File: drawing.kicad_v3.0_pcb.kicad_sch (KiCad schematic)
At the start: 43 parts, among them IC1 DW01A-G, J1 Micro USB Chargeport, J2 Conn_01x03, J3 128x32 I2C OLED, J4 TP4056, J5 MK-12C02, J6 Conn_01x02, Q1 FS8205, U1 HT7333-SOT89, U2 ESP-12E, U3 ATTINY85-20PU

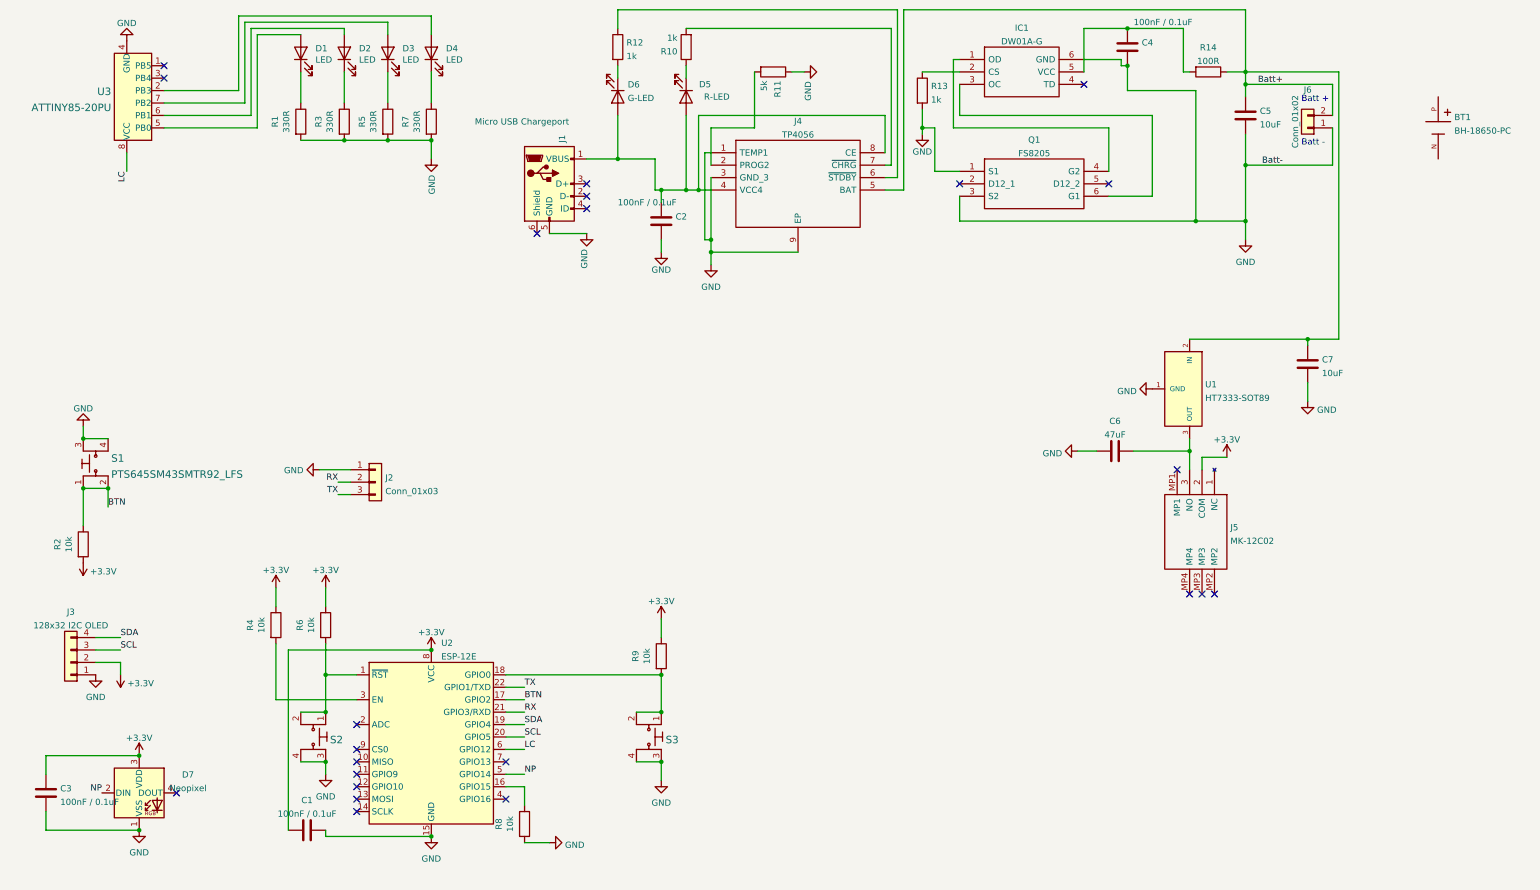
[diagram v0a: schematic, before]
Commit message: Fixed HT7333 and charging circuit
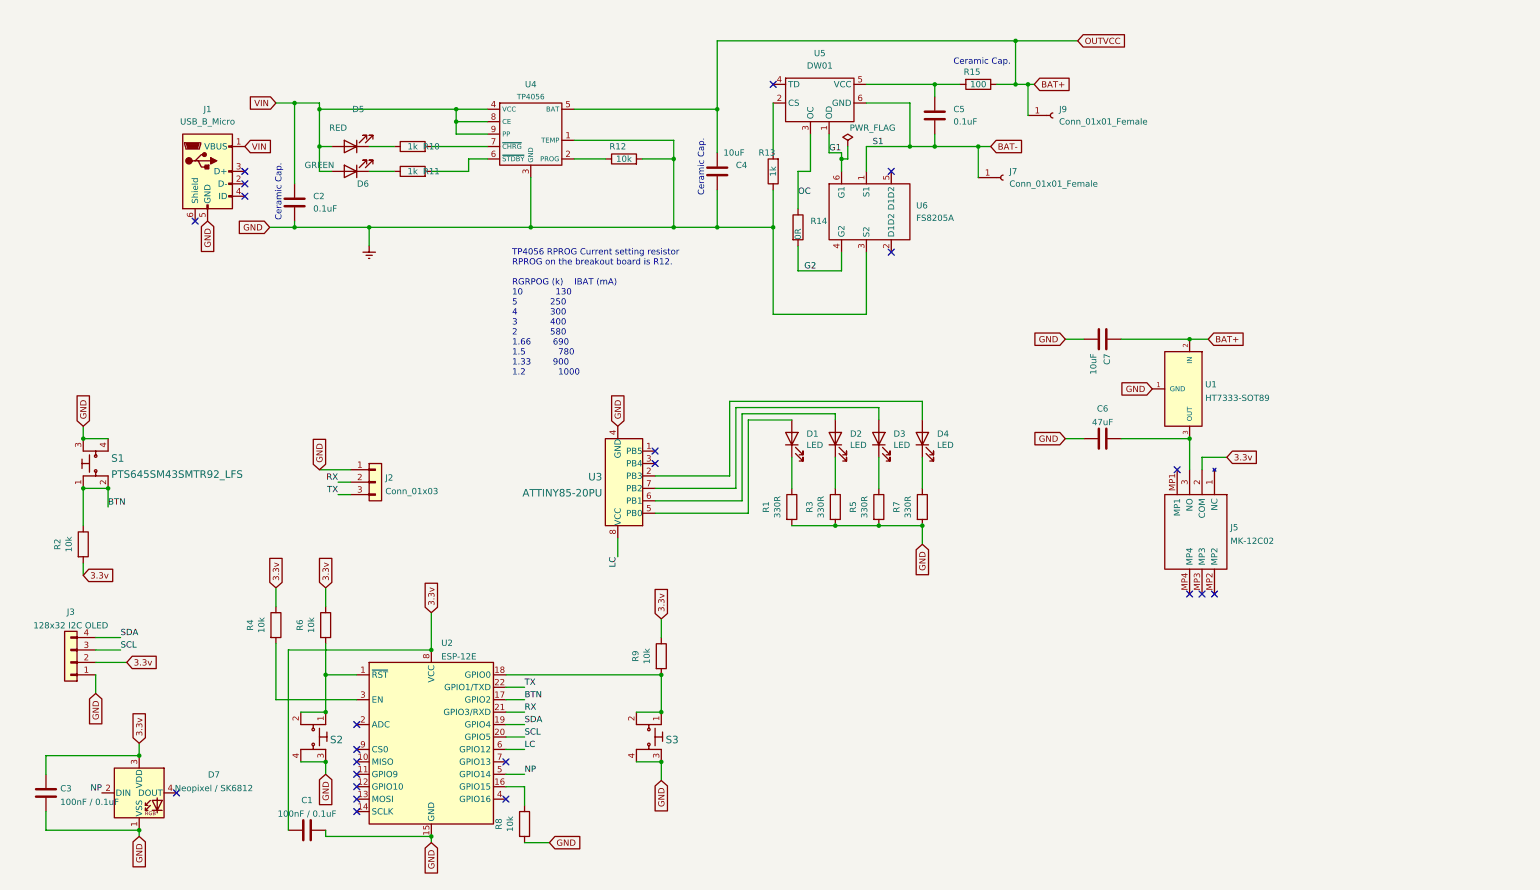
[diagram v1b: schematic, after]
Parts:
- removed BT1: BH-18650-PC, user-footprints:BAT_BH-18650-PC, symbol BH-18650-PC:BH-18650-PC
- removed IC1: DW01A-G, user-footprints:SOT95P280X135-6N, symbol DW01A-G:DW01A-G
- removed J4: TP4056, Custom:SOIC127P600X175-9N, symbol TP4056:TP4056
- removed J6: Conn_01x02, Connector_PinSocket_2.54mm:PinSocket_1x02_P2.54mm_Vertical, symbol Connector_Generic:Conn_01x02
- removed Q1: FS8205, user-footprints:FS8205, symbol FS8205:FS8205
- added J7, J9: Conn_01x01_Female, Connector_PinSocket_2.54mm:PinSocket_1x01_P2.54mm_Vertical, symbol Connector:Conn_01x01_Female
- added R15: 100, Resistor_SMD:R_0805_2012Metric_Pad1.20x1.40mm_HandSolder, symbol Device:R
- added U4: TP4056, Package_SO:SOIC-8-1EP_3.9x4.9mm_P1.27mm_EP2.29x3mm, symbol tp4056:TP4056
- added U5: DW01, Package_TO_SOT_SMD:SOT-23-6_Handsoldering, symbol dw01:DW01
- added U6: FS8205A, Package_TO_SOT_SMD:SOT-23-6_Handsoldering, symbol fs8205:FS8205A
- C2: value 100nF / 0.1uF -> 0.1uF
- C4: value 100nF / 0.1uF -> 10uF
- C5: value 10uF -> 0.1uF
- D5: value R-LED -> RED
- D6: value G-LED -> GREEN
- D7: value Neopixel -> Neopixel / SK6812
- J1: value Micro USB Chargeport -> USB_B_Micro
- R11: value 5k -> 1k
- R12: value 1k -> 10k
- R14: value 100R -> 0R
- U1: footprint Custom:Holtek-HT7333-SOT89-Level_A -> user-footprints:Holtek-HT7333-SOT89-Level_A
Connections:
- net VIN: now reaches D5.2 (A), D6.2 (A), J1.1 (VBUS)
- net VIN: now also C2.1, U4.4 (VCC), U4.8 (CE), U4.9 (PP); no longer C2.2
- net at R12.1: now also U4.2 (PROG)
- net at D6.1 (K): now also R11.1; no longer R12.2
- net BAT+: now reaches C4.1
- net BAT+: now also C7.2, U1.2 (IN), J9.1 (Pin_1), R15.1, U4.5 (BAT); no longer R14.2
- net at R11.2: now also U4.6 (~{STDBY})
- net at R10.2: now also U4.7 (~{CHRG})
- net Earth: now reaches R13.1
- net Earth: now also C1.2, C2.2, C3.1, C4.2, C6.1, C7.1, D7.1 (VSS), J1.5 (GND), J2.1 (Pin_1), J3.1 (Pin_1), R1.2, R12.2, R3.2, R5.2, R7.2, R8.2, S1.3, S1.4, S2.3, S2.4, S3.3, S3.4, U1.1 (GND), U2.15 (GND), U3.4 (GND), U4.1 (TEMP), U4.3 (GND), U6.3 (S2)
- net +3V3 renamed 3.3v
- removed net Batt+: C5.1, C7.2, R14.1, U1.2 (IN)
- removed net GND: C1.2, C2.1, C3.1, C4.2, C5.2, C6.1, C7.1, D7.1 (VSS), J1.5 (GND), J2.1 (Pin_1), J3.1 (Pin_1), R1.2, R11.1, R13.2, R3.2, R5.2, R7.2, R8.2, S1.3, S1.4, S2.3, S2.4, S3.3, S3.4, U1.1 (GND), U2.15 (GND), U3.4 (GND)
- new net: R13.2, U5.2 (CS)
- new net: C5.1, R15.2, U5.5 (VCC)
- new net BAT-: C5.2, J7.1 (Pin_1), U5.6 (GND), U6.1 (S1)
- new net G1: U5.1 (OD), U6.6 (G1)
- new net G2: R14.2, U6.4 (G2)
- new net OC: R14.1, U5.3 (OC)
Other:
- note added: "Ceramic Cap."
- note added: "TP4056 RPROG Current setting resistor RPROG on the breakout board is R12. RGRPOG (k) IBAT (mA) 10 130 5 250 4 300 3 400 2 580 1.66 690 1.5 780 1.33 900 1.2 1000"
- note removed: "Batt +"
- note removed: "Batt -"
- moved on the sheet: C6, C7, D1, D2, D3, D4, R1, R3, R5, R7, U3
